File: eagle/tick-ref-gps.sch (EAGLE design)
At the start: 47 parts, among them CN1 1PPS Out, CN2 ISP, CN3 RS232, CN4 Power In, CN5 Serial Program, U1 ATMEGA168-AU, U2 AS1115, U3 MAX232, U4 LM2931_FIXED, X1 16MHz

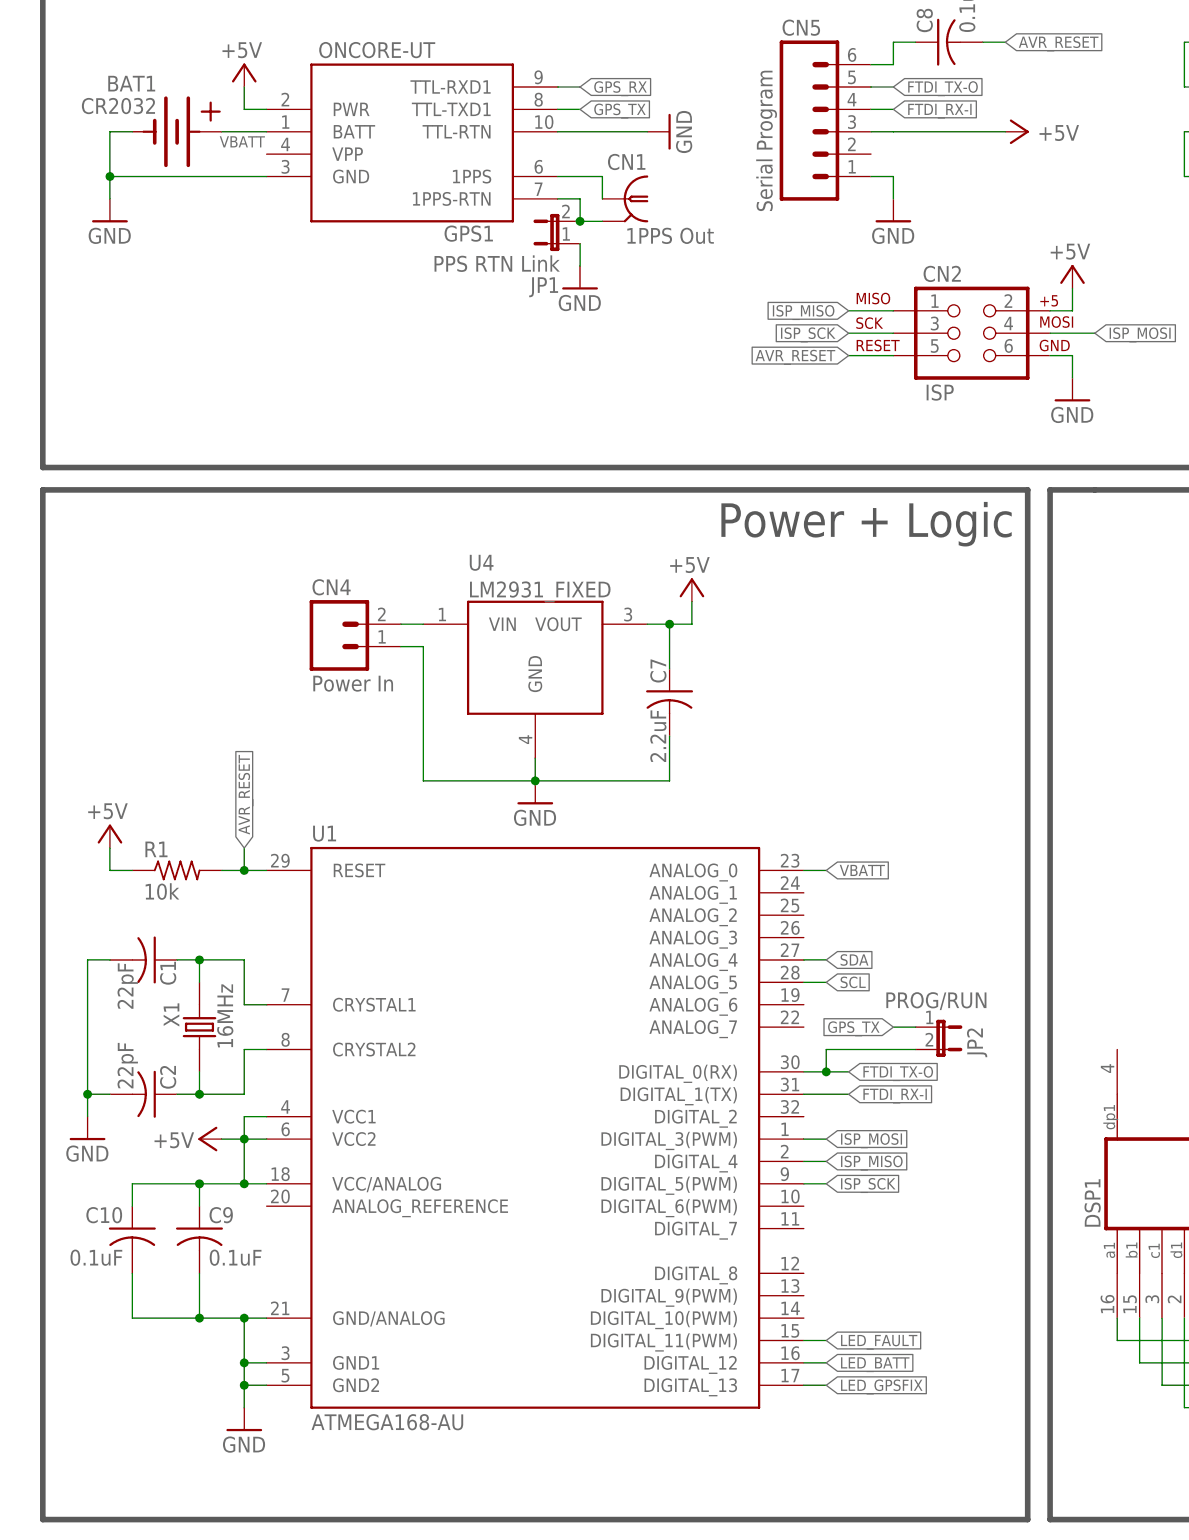
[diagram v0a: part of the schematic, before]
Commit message: Routing in progress, 42 airwires left to route.
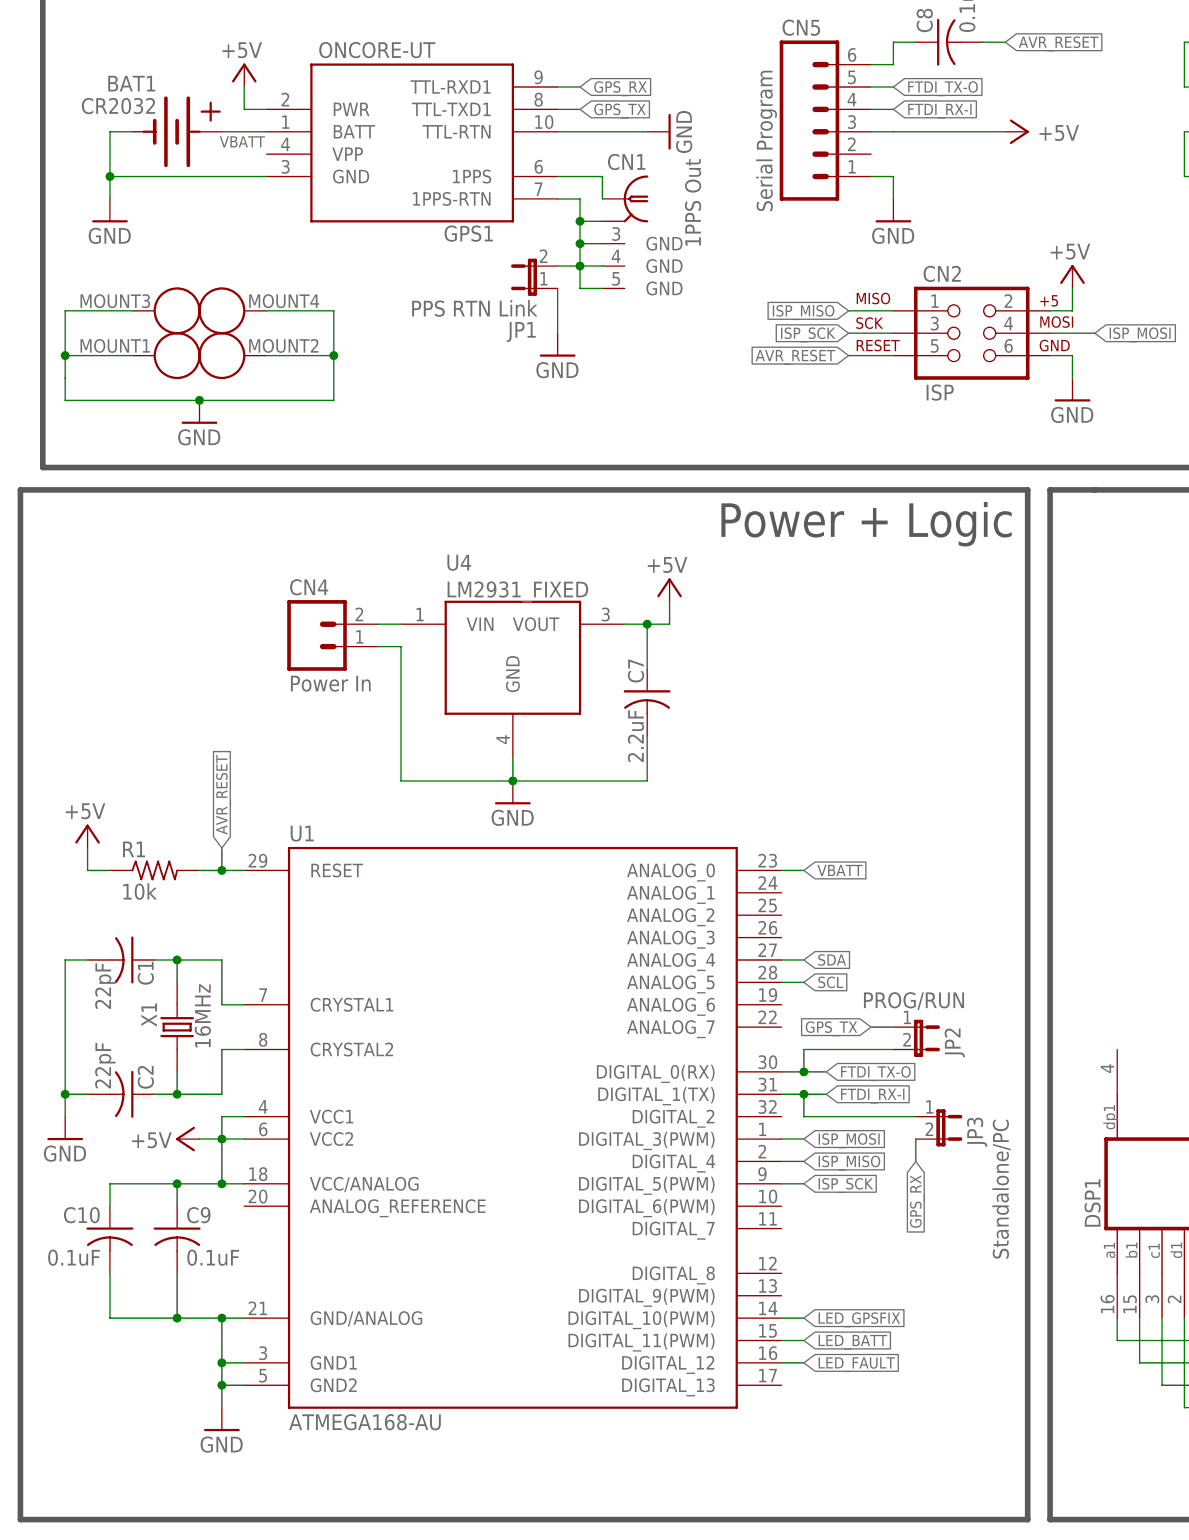
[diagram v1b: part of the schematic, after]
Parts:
- added JP3: Standalone/PC, SparkFun:JUMPER-2SMD-NO
- JP2: device SparkFun:JUMPER-2SMD-NO -> SparkFun:JUMPER-2PTH_LOCK
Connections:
- net 1PPS_RTN: now also CN1G2.GND, CN1G3.GND, CN1G4.GND
- net FTDI_RX-I: now also JP3.1
- net GND: now also GPS1G$2.MOUNTHOLE1, GPS1G$2.MOUNTHOLE2, GPS1G$2.MOUNTHOLE3, GPS1G$2.MOUNTHOLE4
- net GPS_RX: now also JP3.2
- net LED_BATT: now also U1.DIGITAL_11(PWM); no longer U1.DIGITAL_12
- net LED_FAULT: now also U1.DIGITAL_12; no longer U1.DIGITAL_11(PWM)
- net LED_GPSFIX: now also U1.DIGITAL_10(PWM); no longer U1.DIGITAL_13
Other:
- moved on the sheet: C1, C10, C2, C7, C9, CN4, JP1, JP2, R1, U1, U4, X1

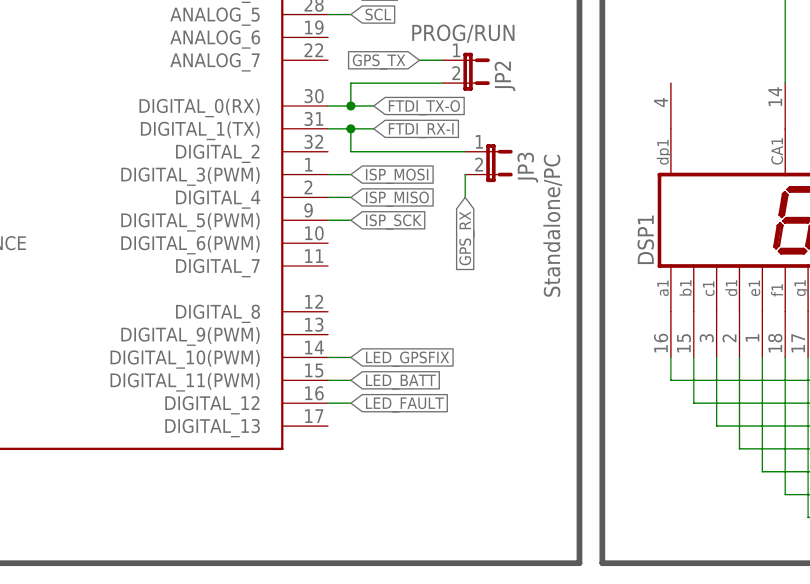
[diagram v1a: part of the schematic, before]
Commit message: Completed routing, pending silk and checklist.
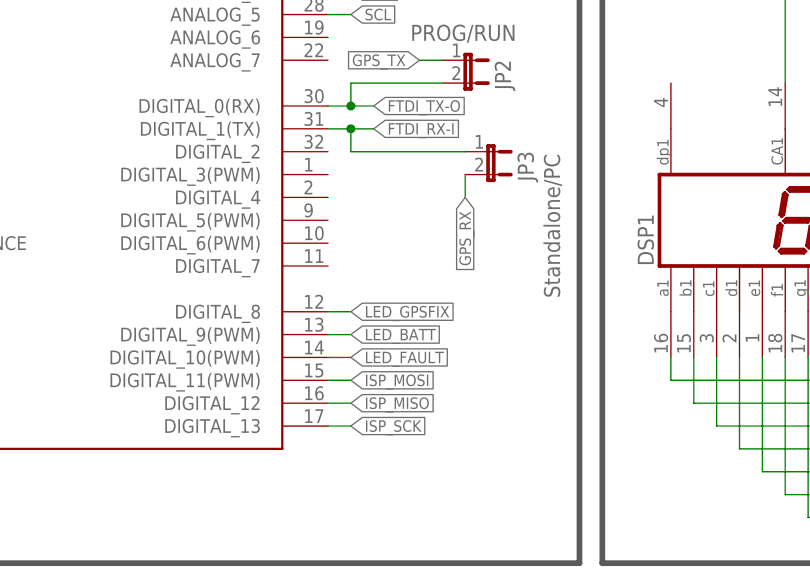
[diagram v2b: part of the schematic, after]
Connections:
- net ISP_MISO: now also U1.DIGITAL_12; no longer U1.DIGITAL_4
- net ISP_MOSI: now also U1.DIGITAL_11(PWM); no longer U1.DIGITAL_3(PWM)
- net ISP_SCK: now also U1.DIGITAL_13; no longer U1.DIGITAL_5(PWM)
- net LED_BATT: now also U1.DIGITAL_9(PWM); no longer U1.DIGITAL_11(PWM)
- net LED_FAULT: now also U1.DIGITAL_10(PWM); no longer U1.DIGITAL_12
- net LED_GPSFIX: now also U1.DIGITAL_8; no longer U1.DIGITAL_10(PWM)
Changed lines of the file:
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@@
 <grid distance="0.1" unitdist="inch" unit="inch" style="lines" multiple="1" display="no" altdistance="0.01" altunitdist="inch" altunit="inch"/>
 <layers>
-<layer number="1" name="Top" color="4" fill="1" visible="yes" active="no"/>
-<layer number="2" name="Route2" color="1" fill="3" visible="yes" active="no"/>
-<layer number="3" name="Route3" color="4" fill="3" visible="yes" active="no"/>
-<layer number="14" name="Route14" color="1" fill="6" visible="yes" active="no"/>
-<layer number="15" name="Route15" color="4" fill="6" visible="yes" active="no"/>
-<layer number="16" name="Bottom" color="1" fill="1" visible="yes" active="no"/>
-<layer number="17" name="Pads" color="2" fill="1" visible="yes" active="no"/>
-<layer number="18" name="Vias" color="2" fill="1" visible="yes" active="no"/>
-<layer number="19" name="Unrouted" color="6" fill="1" visible="yes" active="no"/>
-<layer number="20" name="Dimension" color="15" fill="1" visible="yes" active="no"/>
-<layer number="21" name="tPlace" color="7" fill="1" visible="yes" active="no"/>
-<layer number="22" name="bPlace" color="7" fill="1" visible="yes" active="no"/>
-<layer number="23" name="tOrigins" color="15" fill="1" visible="yes" active="no"/>
-<layer number="24" name="bOrigins" color="15" fill="1" visible="yes" active="no"/>
-<layer number="25" name="tNames" color="7" fill="1" visible="yes" active="no"/>
-<layer number="26" name="bNames" color="7" fill="1" visible="yes" active="no"/>
-<layer number="27" name="tValues" color="7" fill="1" visible="yes" active="no"/>
-<layer number="28" name="bValues" color="7" fill="1" visible="yes" active="no"/>
+<layer number="1" name="Top" color="4" fill="1" visible="no" active="no"/>
+<layer number="2" name="Route2" color="1" fill="3" visible="no" active="no"/>
+<layer number="3" name="Route3" color="4" fill="3" visible="no" active="no"/>
+<layer number="14" name="Route14" color="1" fill="6" visible="no" active="no"/>
+<layer number="15" name="Route15" color="4" fill="6" visible="no" active="no"/>
+<layer number="16" name="Bottom" color="1" fill="1" visible="no" active="no"/>
+<layer number="17" name="Pads" color="2" fill="1" visible="no" active="no"/>
+<layer number="18" name="Vias" color="2" fill="1" visible="no" active="no"/>
+<layer number="19" name="Unrouted" color="6" fill="1" visible="no" active="no"/>
+<layer number="20" name="Dimension" color="15" fill="1" visible="no" active="no"/>
+<layer number="21" name="tPlace" color="7" fill="1" visible="no" active="no"/>
+<layer number="22" name="bPlace" color="7" fill="1" visible="no" active="no"/>
+<layer number="23" name="tOrigins" color="15" fill="1" visible="no" active="no"/>
+<layer number="24" name="bOrigins" color="15" fill="1" visible="no" active="no"/>
+<layer number="25" name="tNames" color="7" fill="1" visible="no" active="no"/>
+<layer number="26" name="bNames" color="7" fill="1" visible="no" active="no"/>
+<layer number="27" name="tValues" color="7" fill="1" visible="no" active="no"/>
+<layer number="28" name="bValues" color="7" fill="1" visible="no" active="no"/>
 <layer number="29" name="tStop" color="7" fill="3" visible="no" active="no"/>
 <layer number="30" name="bStop" color="7" fill="6" visible="no" active="no"/>
@@
 <layer number="35" name="tGlue" color="7" fill="4" visible="no" active="no"/>
 <layer number="36" name="bGlue" color="7" fill="5" visible="no" active="no"/>
-<layer number="37" name="tTest" color="7" fill="1" visible="yes" active="no"/>
-<layer number="38" name="bTest" color="7" fill="1" visible="yes" active="no"/>
+<layer number="37" name="tTest" color="7" fill="1" visible="no" active="no"/>
+<layer number="38" name="bTest" color="7" fill="1" visible="no" active="no"/>
 <layer number="39" name="tKeepout" color="4" fill="11" visible="no" active="no"/>
 <layer number="40" name="bKeepout" color="1" fill="11" visible="no" active="no"/>
@@
 <layer number="44" name="Drills" color="7" fill="1" visible="no" active="no"/>
 <layer number="45" name="Holes" color="7" fill="1" visible="no" active="no"/>
-<layer number="46" name="Milling" color="3" fill="1" visible="yes" active="no"/>
-<layer number="47" name="Measures" color="7" fill="1" visible="yes" active="no"/>
-<layer number="48" name="Document" color="7" fill="1" visible="yes" active="no"/>
-<layer number="49" name="Reference" color="7" fill="1" visible="yes" active="no"/>
-<layer number="50" name="dxf" color="7" fill="1" visible="yes" active="no"/>
-<layer number="51" name="tDocu" color="7" fill="1" visible="yes" active="no"/>
-<layer number="52" name="bDocu" color="7" fill="1" visible="yes" active="no"/>
-<layer number="53" name="tGND_GNDA" color="7" fill="9" visible="yes" active="no"/>
-<layer number="54" name="bGND_GNDA" color="1" fill="9" visible="yes" active="no"/>
-<layer number="56" name="wert" color="7" fill="1" visible="yes" active="no"/>
+<layer number="46" name="Milling" color="3" fill="1" visible="no" active="no"/>
+<layer number="47" name="Measures" color="7" fill="1" visible="no" active="no"/>
+<layer number="48" name="Document" color="7" fill="1" visible="no" active="no"/>
+<layer number="49" name="Reference" color="7" fill="1" visible="no" active="no"/>
+<layer number="50" name="dxf" color="7" fill="1" visible="no" active="no"/>
+<layer number="51" name="tDocu" color="7" fill="1" visible="no" active="no"/>
+<layer number="52" name="bDocu" color="7" fill="1" visible="no" active="no"/>
+<layer number="53" name="tGND_GNDA" color="7" fill="9" visible="no" active="no"/>
+<layer number="54" name="bGND_GNDA" color="1" fill="9" visible="no" active="no"/>
+<layer number="56" name="wert" color="7" fill="1" visible="no" active="no"/>
 <layer number="91" name="Nets" color="2" fill="1" visible="yes" active="yes"/>
 <layer number="92" name="Busses" color="1" fill="1" visible="yes" active="yes"/>
@@
 <net name="LED_GPSFIX" class="0">
 <segment>
-<label x="86.36" y="22.86" size="1.27" layer="95" xref="yes"/>
-<pinref part="U1" gate="1" pin="DIGITAL_10(PWM)"/>
-<wire x1="83.82" y1="22.86" x2="86.36" y2="22.86" width="0.1524" layer="91"/>
+<label x="86.36" y="27.94" size="1.27" layer="95" xref="yes"/>
+<pinref part="U1" gate="1" pin="DIGITAL_8"/>
+<wire x1="83.82" y1="27.94" x2="86.36" y2="27.94" width="0.1524" layer="91"/>
 </segment>
 <segment>
@@
 </segment>
 <segment>
-<pinref part="U1" gate="1" pin="DIGITAL_11(PWM)"/>
-<wire x1="83.82" y1="20.32" x2="86.36" y2="20.32" width="0.1524" layer="91"/>
-<label x="86.36" y="20.32" size="1.27" layer="95" xref="yes"/>
+<label x="86.36" y="25.4" size="1.27" layer="95" xref="yes"/>
+<pinref part="U1" gate="1" pin="DIGITAL_9(PWM)"/>
+<wire x1="83.82" y1="25.4" x2="86.36" y2="25.4" width="0.1524" layer="91"/>
 </segment>
 </net>
@@
 </segment>
 <segment>
-<pinref part="U1" gate="1" pin="DIGITAL_5(PWM)"/>
-<wire x1="83.82" y1="38.1" x2="86.36" y2="38.1" width="0.1524" layer="91"/>
-<label x="86.36" y="38.1" size="1.27" layer="95" xref="yes"/>
+<label x="86.36" y="15.24" size="1.27" layer="95" xref="yes"/>
+<pinref part="U1" gate="1" pin="DIGITAL_13"/>
+<wire x1="83.82" y1="15.24" x2="86.36" y2="15.24" width="0.1524" layer="91"/>
 </segment>
 </net>
@@
 </segment>
 <segment>
-<pinref part="U1" gate="1" pin="DIGITAL_4"/>
-<wire x1="83.82" y1="40.64" x2="86.36" y2="40.64" width="0.1524" layer="91"/>
-<label x="86.36" y="40.64" size="1.27" layer="95" xref="yes"/>
+<label x="86.36" y="17.78" size="1.27" layer="95" xref="yes"/>
+<pinref part="U1" gate="1" pin="DIGITAL_12"/>
+<wire x1="86.36" y1="17.78" x2="83.82" y2="17.78" width="0.1524" layer="91"/>
 </segment>
 </net>
@@
 </segment>
 <segment>
-<pinref part="U1" gate="1" pin="DIGITAL_3(PWM)"/>
-<wire x1="83.82" y1="43.18" x2="86.36" y2="43.18" width="0.1524" layer="91"/>
-<label x="86.36" y="43.18" size="1.27" layer="95" xref="yes"/>
+<label x="86.36" y="20.32" size="1.27" layer="95" xref="yes"/>
+<pinref part="U1" gate="1" pin="DIGITAL_11(PWM)"/>
+<wire x1="86.36" y1="20.32" x2="83.82" y2="20.32" width="0.1524" layer="91"/>
 </segment>
 </net>
@@
 </segment>
 <segment>
-<label x="86.36" y="17.78" size="1.27" layer="95" xref="yes"/>
-<pinref part="U1" gate="1" pin="DIGITAL_12"/>
-<wire x1="83.82" y1="17.78" x2="86.36" y2="17.78" width="0.1524" layer="91"/>
-</segment>
-</net>
+<label x="86.36" y="22.86" size="1.27" layer="95" xref="yes"/>
+<pinref part="U1" gate="1" pin="DIGITAL_10(PWM)"/>
+<wire x1="83.82" y1="22.86" x2="86.36" y2="22.86" width="0.1524" layer="91"/>
+</segment>
+</net>
